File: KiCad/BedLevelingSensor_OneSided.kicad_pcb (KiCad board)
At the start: 2 copper layers, 11.2 x 19.7 mm, 9 parts, among them J1 SOLENOID, J2 Sensor, J3 Input, U1 ATTINY15-1SC, U2 L9110

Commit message: Schematic/PCB adjust
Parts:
- removed J3: Input, Connectors:GS3
- added J6: Inp_data, Connectors:GS2, F.Cu at (141.2, 107.8)
- R2: value 10K -> 1K
- moved D1 14.2 mm to (141.7, 124.2)
- moved R2 4.85 mm to (136.3, 107.6), turned to 180 degrees
- moved J2 0.92 mm to (133.5, 108.6), turned to 0 degrees
- moved R3 0.52 mm to (142.0, 114.8), turned to 90 degrees
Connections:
- net LED renamed MISO
- net Net-(R1-Pad2) renamed RST
- D1 pad 1: GND -> Net-(D1-Pad1)
- D1 pad 2: Net-(D1-Pad2) -> VCC
- J2 pad 2: Net-(J2-Pad2) -> GND
- R2 pad 1: GND -> SCK
- R2 pad 2: Net-(J2-Pad2) -> Net-(J2-Pad1)
- R3 pad 1: Net-(D1-Pad2) -> Net-(D1-Pad1)
- U1 pad 5: Net-(J3-Pad3) -> MOSI
- U1 pad 7: Net-(J2-Pad1) -> SCK
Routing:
- net Net-(D1-Pad1): track 0.00 -> 7.72 mm
- net VCC: track 7.46 -> 13.9 mm
- net Net-(J3-Pad3): track 4.99 -> 0.00 mm
- net MOSI: track 0.00 -> 4.17 mm
- net MISO: track 6.48 -> 9.87 mm
- net SCK: track 0.00 -> 3.03 mm
- net Net-(J2-Pad1): track 4.07 -> 1.85 mm
- net Net-(J2-Pad2): track 2.21 -> 0.00 mm
- net Net-(D1-Pad2): track 2.12 -> 0.00 mm
- net GND: track 23.0 -> 22.4 mm, vias 2 -> 1
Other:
- board size 11.2 x 19.7 mm -> 11.2 x 21 mm

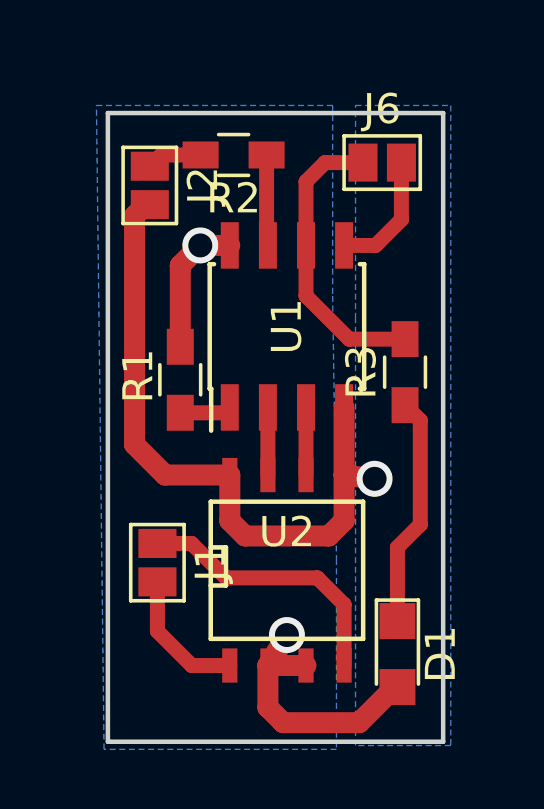
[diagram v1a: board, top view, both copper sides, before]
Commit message: adjust attiny footprint
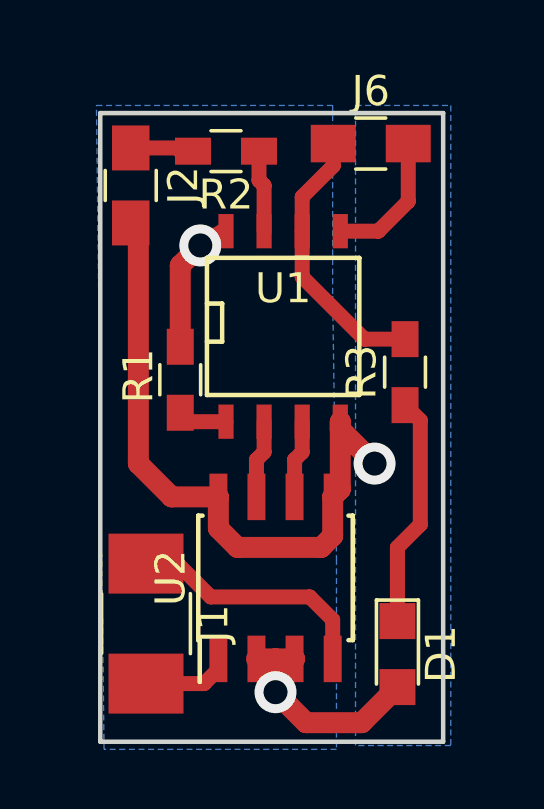
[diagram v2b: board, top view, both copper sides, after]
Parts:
- J1: footprint Connectors:GS2 -> Capacitors_SMD:C_1210_HandSoldering
- J2, J6: footprint Connectors:GS2 -> Capacitors_SMD:C_0805_HandSoldering
- U1: footprint Housings_SOIC:SOIC-8_3.9x4.9mm_Pitch1.27mm -> SMD_Packages:SOIC-8-N
- U2: footprint SMD_Packages:SOIC-8-N -> Housings_SOIC:SOIC-8_3.9x4.9mm_Pitch1.27mm
- moved J1 2.07 mm to (133.3, 123.2), turned to 270 degrees
- moved J6 0.74 mm to (140.8, 107.2), turned to 0 degrees
- moved J2 0.63 mm to (132.8, 108.6), turned to 270 degrees
- moved U2 0.46 mm to (137.7, 121.7), turned to 90 degrees
- moved R2 0.28 mm to (136.0, 107.4)
- moved U1 0.13 mm to (137.9, 113.3), turned to 0 degrees
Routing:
- net Net-(J1-Pad2): track 4.53 -> 2.96 mm
- net Net-(J1-Pad1): track 9.10 -> 8.30 mm
- net MISO: track 9.87 -> 9.16 mm
- net VCC: track 13.9 -> 14.4 mm
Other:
- board size 11.2 x 21 mm -> 11.4 x 21 mm
- net class Default: via_dia 1.2 -> 1.4
- net class POWER: via_dia 1.2 -> 1.4
